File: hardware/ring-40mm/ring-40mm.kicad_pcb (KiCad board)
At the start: 2 copper layers, 40.2 x 46.4 mm, 44 parts, among them J1 Conn_01x03, J2 Conn_01x03

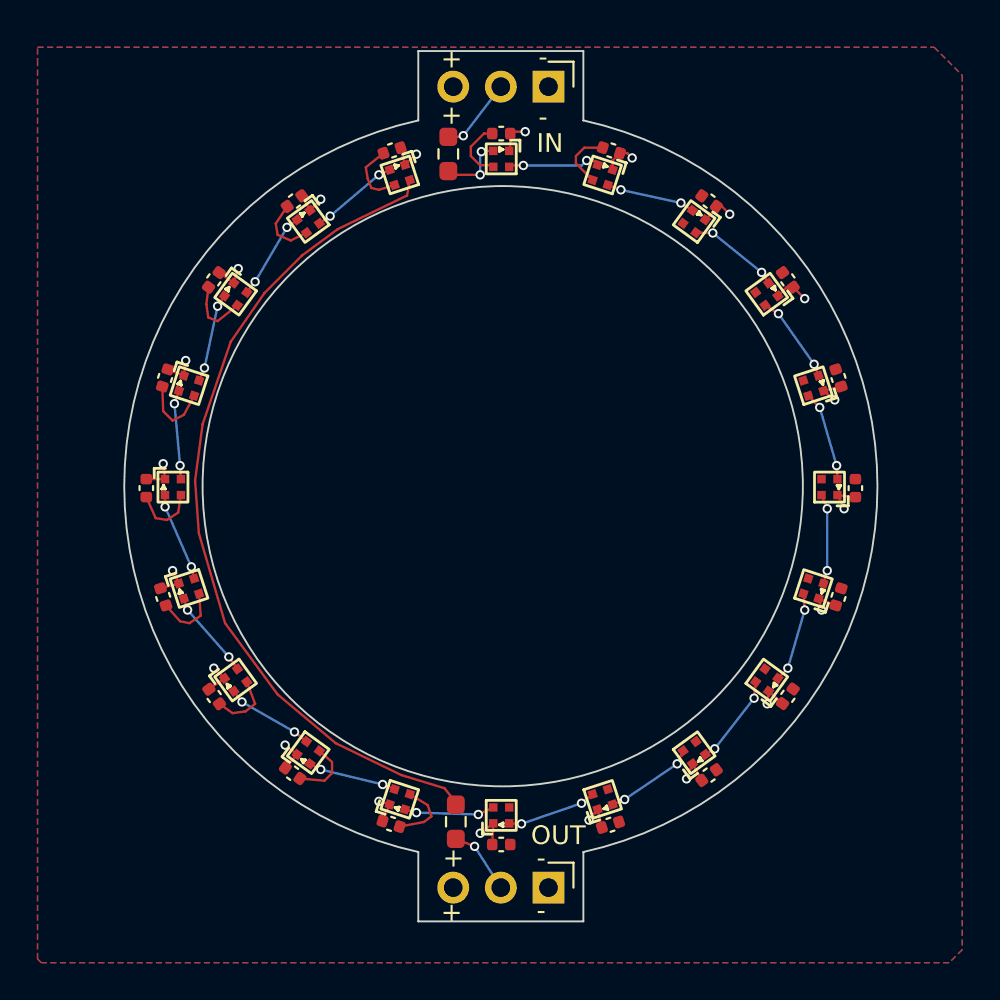
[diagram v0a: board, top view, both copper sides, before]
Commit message: ring-40mm: clean up and generate fab files
Change-Id: I3ff063815f256b7ba3f7e43d15cf4eef6ca098e3
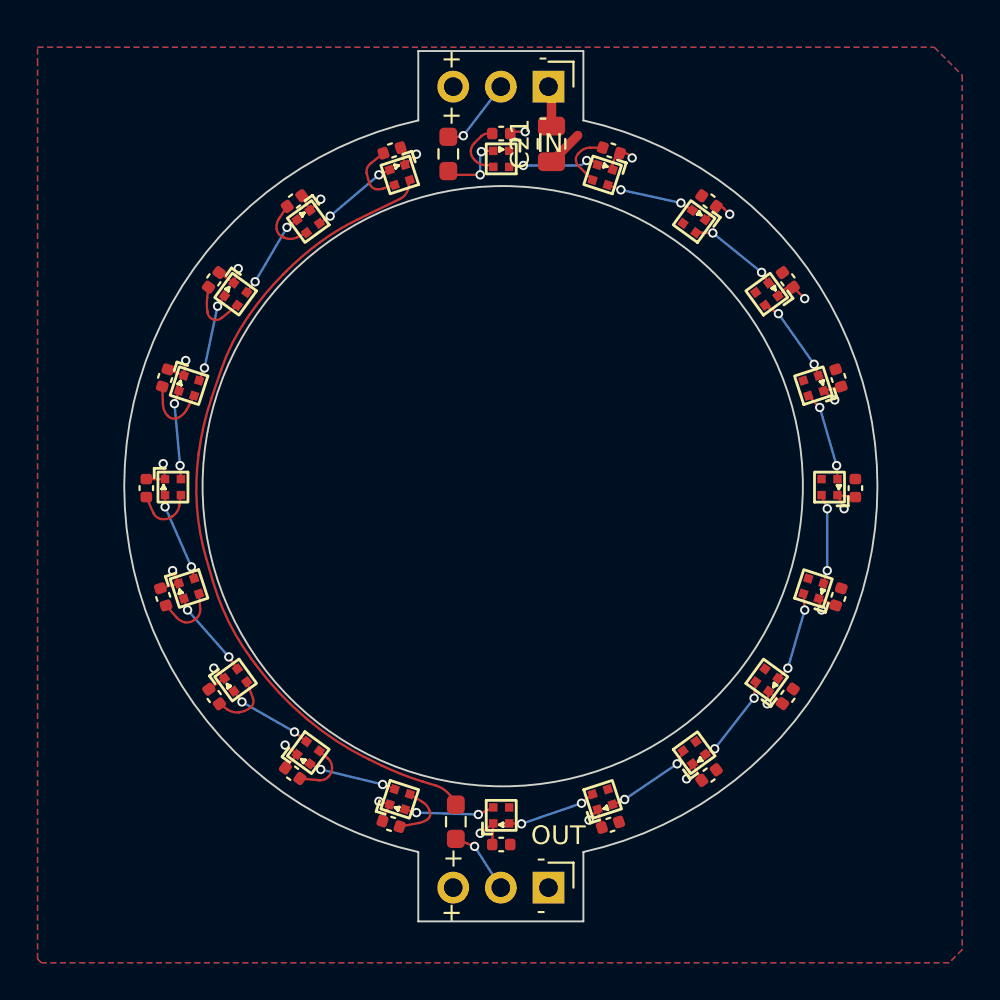
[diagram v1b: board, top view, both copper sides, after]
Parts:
- added C21: 22uF, Capacitor_SMD:C_0805_2012Metric, F.Cu at (102.6, 81.8)
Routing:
- net GND: track 35.1 -> 37.2 mm
- net VCC: track 38.4 -> 39.0 mm

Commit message: Update ring-40mm to v1.1:
- Remove thermal relief for SMD pads
- Update silkscreen to be more readable

Change-Id: I3b8c40db7d677df12dd3b0feafd79e9c8012d25c
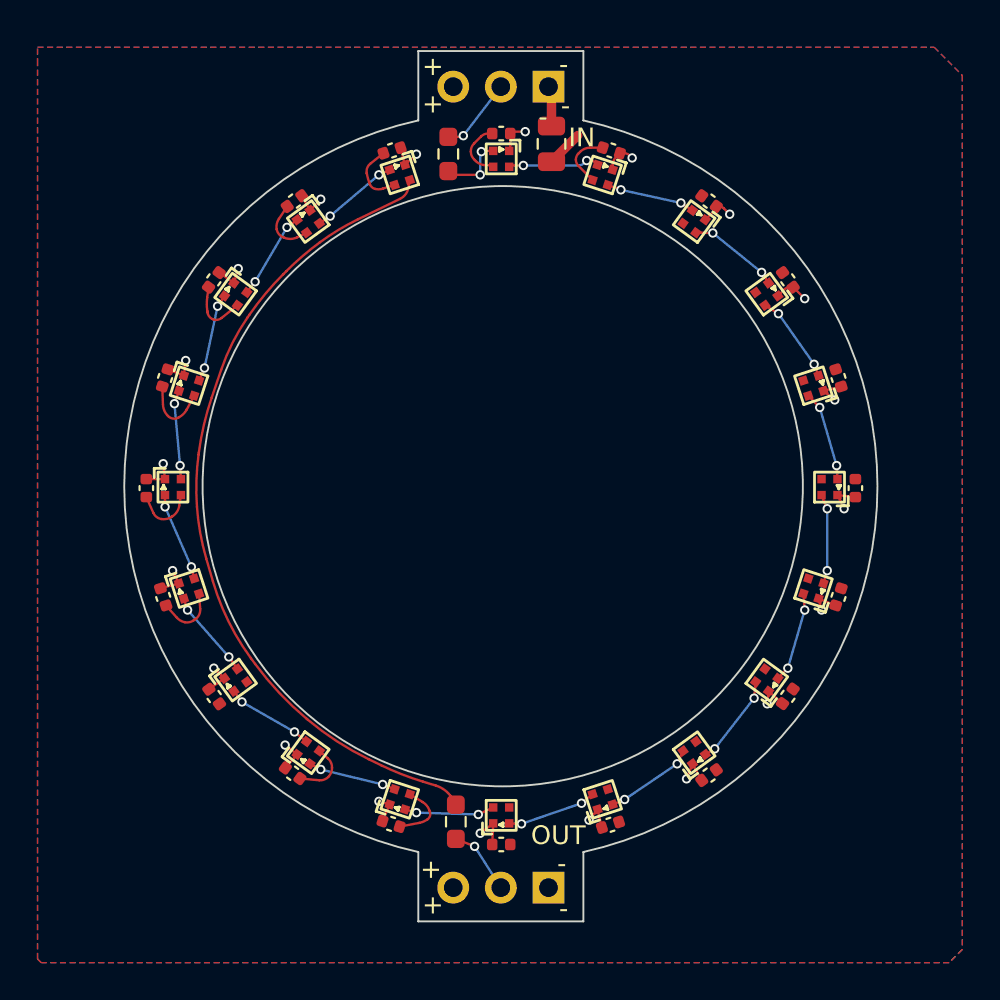
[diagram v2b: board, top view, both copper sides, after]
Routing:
- net VCC: track 39.0 -> 35.7 mm
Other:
- board text added: "v1.1"
- board text removed: "v1.0"
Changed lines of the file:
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@@
         (effects (font (size 1 1) (thickness 0.15)))
     )
-    (fp_line (start -1.33 -1.33) (end 0 -1.33)
-      (stroke (width 0.12) (type solid)) (layer "F.SilkS"))
-    (fp_line (start -1.33 0) (end -1.33 -1.33)
-      (stroke (width 0.12) (type solid)) (layer "F.SilkS"))
     (fp_line (start -1.8 -1.8) (end -1.8 6.85)
       (stroke (width 0.05) (type solid)) (layer "F.CrtYd"))
@@
     (property "ki_keywords" "cap capacitor")
     (attr smd)
-    (fp_text reference "C21" (at 0 -1.68 90) (layer "F.SilkS")
+    (fp_text reference "C21" (at 0 -1.68 90) (layer "F.SilkS") hide
         (effects (font (size 1 1) (thickness 0.15)))
     )
@@
         (effects (font (size 1 1) (thickness 0.15)))
     )
-    (fp_line (start -1.33 -1.33) (end 0 -1.33)
-      (stroke (width 0.12) (type solid)) (layer "F.SilkS"))
-    (fp_line (start -1.33 0) (end -1.33 -1.33)
-      (stroke (width 0.12) (type solid)) (layer "F.SilkS"))
     (fp_line (start -1.8 -1.8) (end -1.8 6.85)
       (stroke (width 0.05) (type solid)) (layer "F.CrtYd"))
@@
   (gr_circle (center 100 100) (end 116 100)
     (stroke (width 0.1) (type default)) (fill none) (layer "Edge.Cuts"))
-  (gr_text "IN" (at 100.6 81.2) (layer "B.SilkS")
+  (gr_text "IN" (at 101.1 81.7) (layer "B.SilkS")
+    (effects (font (size 1.5 1.5) (thickness 0.2)) (justify left bottom mirror))
+  )
+  (gr_text "+" (at 98.3 120.5) (layer "B.SilkS")
+    (effects (font (size 1.5 1.5) (thickness 0.2)) (justify left bottom mirror))
+  )
+  (gr_text "+" (at 98.2 81.2) (layer "B.SilkS")
+    (effects (font (size 1.5 1.5) (thickness 0.2)) (justify left bottom mirror))
+  )
+  (gr_text "v1.1" (at 119.6 97.2 90) (layer "B.SilkS")
     (effects (font (size 1 1) (thickness 0.15)) (justify left bottom mirror))
   )
-  (gr_text "+" (at 98 120.4) (layer "B.SilkS")
-    (effects (font (size 1 1) (thickness 0.15)) (justify left bottom mirror))
-  )
-  (gr_text "+" (at 98 80.8) (layer "B.SilkS")
-    (effects (font (size 1 1) (thickness 0.15)) (justify left bottom mirror))
-  )
-  (gr_text "v1.0" (at 119.6 97.2 90) (layer "B.SilkS")
-    (effects (font (size 1 1) (thickness 0.15)) (justify left bottom mirror))
-  )
-  (gr_text "-" (at 103.1 80.9) (layer "B.SilkS")
-    (effects (font (size 1 1) (thickness 0.15)) (justify left bottom mirror))
-  )
-  (gr_text "-" (at 103 120.5) (layer "B.SilkS")
-    (effects (font (size 1 1) (thickness 0.15)) (justify left bottom mirror))
-  )
-  (gr_text "OUT" (at 101.4 120.1) (layer "B.SilkS")
-    (effects (font (size 1 1) (thickness 0.15)) (justify left bottom mirror))
-  )
-  (gr_text "+" (at 96.7 77.8) (layer "F.SilkS")
-    (effects (font (size 1 1) (thickness 0.15)) (justify left bottom))
+  (gr_text "-" (at 103.5 81.3) (layer "B.SilkS")
+    (effects (font (size 1.5 1.5) (thickness 0.2)) (justify left bottom mirror))
+  )
+  (gr_text "-" (at 103.3 120.5) (layer "B.SilkS")
+    (effects (font (size 1.5 1.5) (thickness 0.2)) (justify left bottom mirror))
+  )
+  (gr_text "OUT" (at 101.9 119.3) (layer "B.SilkS")
+    (effects (font (size 1.5 1.5) (thickness 0.2)) (justify left bottom mirror))
   )
   (gr_text "OUT" (at 101.5 119.2) (layer "F.SilkS")
     (effects (font (size 1 1) (thickness 0.15)) (justify left bottom))
   )
-  (gr_text "-" (at 101.8 123.2) (layer "F.SilkS")
+  (gr_text "-" (at 103 123.1) (layer "F.SilkS")
     (effects (font (size 1 1) (thickness 0.15)) (justify left bottom))
   )
-  (gr_text "-" (at 101.8 120.4) (layer "F.SilkS")
+  (gr_text "-" (at 102.9 120.7) (layer "F.SilkS")
     (effects (font (size 1 1) (thickness 0.15)) (justify left bottom))
   )
-  (gr_text "+" (at 96.8 120.4) (layer "F.SilkS")
+  (gr_text "+" (at 95.6 121) (layer "F.SilkS")
+    (effects (font (size 1 1) (thickness 0.15)) (justify left bottom))
+  )
+  (gr_text "+" (at 95.7 78.2) (layer "F.SilkS")
     (effects (font (size 1 1) (thickness 0.15)) (justify left bottom))
   )
@@
     (effects (font (size 1 1) (thickness 0.15)) (justify left bottom))
   )
-  (gr_text "+" (at 96.7 80.8) (layer "F.SilkS")
+  (gr_text "-" (at 103.1 80.3) (layer "F.SilkS")
     (effects (font (size 1 1) (thickness 0.15)) (justify left bottom))
   )
-  (gr_text "-" (at 101.9 77.7) (layer "F.SilkS")
+  (gr_text "+" (at 95.7 80.2) (layer "F.SilkS")
     (effects (font (size 1 1) (thickness 0.15)) (justify left bottom))
   )
-  (gr_text "IN" (at 101.8 82.3) (layer "F.SilkS")
+  (gr_text "-" (at 103 78.1) (layer "F.SilkS")
     (effects (font (size 1 1) (thickness 0.15)) (justify left bottom))
   )
-  (gr_text "+" (at 96.7 123.3) (layer "F.SilkS")
+  (gr_text "IN" (at 103.5 82) (layer "F.SilkS")
+    (effects (font (size 1 1) (thickness 0.15)) (justify left bottom))
+  )
+  (gr_text "+" (at 95.7 122.9) (layer "F.SilkS")
     (effects (font (size 1 1) (thickness 0.15)) (justify left bottom))
   )
@@
   (segment (start 104.514928 83.4001) (end 104.036178 82.92135) (width 0.127) (layer "F.Cu") (net 1))
   (segment (start 83.599999 107.099999) (end 83.512132 107.158578) (width 0.127) (layer "F.Cu") (net 1))
-  (segment (start 85.949999 112.049999) (end 85.983061 112.045276) (width 0.127) (layer "F.Cu") (net 1))
   (segment (start 99.22 81.2) (end 99.44 81.2) (width 0.127) (layer "F.Cu") (net 1))
   (segment (start 93.59694 84.139054) (end 94.239453 83.940221) (width 0.127) (layer "F.Cu") (net 1))
-  (segment (start 85.312301 111.894501) (end 84.9 111.6) (width 0.127) (layer "F.Cu") (net 1))
   (segment (start 88.06866 85.746911) (end 88.511672 85.082137) (width 0.127) (layer "F.Cu") (net 1))
   (segment (start 82.755774 101.043784) (end 82.845118 100.47318) (width 0.127) (layer "F.Cu") (net 1))
@@
   (segment (start 83.158584 95.904448) (end 83.549495 95.175913) (width 0.127) (layer "F.Cu") (net 1))
   (segment (start 104.036178 82.263821) (end 104.124164 82.175836) (width 0.127) (layer "F.Cu") (net 1))
-  (segment (start 86.686532 111.300625) (end 86.355961 110.428444) (width 0.127) (layer "F.Cu") (net 1))
   (segment (start 81.376017 101.422279) (end 81 100.58) (width 0.127) (layer "F.Cu") (net 1))
   (segment (start 92.937875 82.810486) (end 93.643493 82.248328) (width 0.127) (layer "F.Cu") (net 1))
@@
   (arc (start 98.3 82.15) (mid 98.345942 82.380969) (end 98.476776 82.576776) (width 0.127) (layer "F.Cu") (net 1))
   (arc (start 83.05 107.25) (mid 83.290158 107.250251) (end 83.512132 107.158578) (width 0.127) (layer "F.Cu") (net 1))
-  (arc (start 86.55 111.8) (mid 86.282964 111.960624) (end 85.983061 112.045276) (width 0.127) (layer "F.Cu") (net 1))
-  (arc (start 85.312301 111.894501) (mid 85.616154 112.033748) (end 85.949999 112.049999) (width 0.127) (layer "F.Cu") (net 1))
   (arc (start 98.567111 82.667111) (mid 98.81067 82.829852) (end 99.097969 82.887) (width 0.127) (layer "F.Cu") (net 1))
   (arc (start 96 117.75) (mid 95.78847 117.873937) (end 95.554474 117.947088) (width 0.127) (layer "F.Cu") (net 1))
@@
   (arc (start 96.120943 117.362829) (mid 96.122965 117.575936) (end 96 117.75) (width 0.127) (layer "F.Cu") (net 1))
   (arc (start 82.63038 107.00966) (mid 82.820627 107.163985) (end 83.05 107.25) (width 0.127) (layer "F.Cu") (net 1))
-  (arc (start 86.686532 111.300625) (mid 86.699512 111.572525) (end 86.55 111.8) (width 0.127) (layer "F.Cu") (net 1))
   (arc (start 98.476776 81.723223) (mid 98.345942 81.91903) (end 98.3 82.15) (width 0.127) (layer "F.Cu") (net 1))
   (arc (start 84.261921 90.733447) (mid 84.356793 90.955365) (end 84.55 91.1) (width 0.127) (layer "F.Cu") (net 1))
@@
   (segment (start 98.5 119.2) (end 99.9 121.4) (width 0.127) (layer "B.Cu") (net 25))
   (zone (net 1) (net_name "VCC") (layer "F.Cu") (hatch edge 0.5)
-    (connect_pads (clearance 0.4))
+    (connect_pads thru_hole_only (clearance 0.3))
     (min_thickness 0.2) (filled_areas_thickness no)
     (fill yes (thermal_gap 0.5) (thermal_bridge_width 0.5))
@@
   )
   (zone (net 2) (net_name "GND") (layer "B.Cu") (hatch edge 0.5)
-    (connect_pads (clearance 0.4))
+    (connect_pads thru_hole_only (clearance 0.3))
     (min_thickness 0.2) (filled_areas_thickness no)
     (fill yes (thermal_gap 0.5) (thermal_bridge_width 0.5))
